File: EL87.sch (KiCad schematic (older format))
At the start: 289 parts, among them SW1 ESC, SW10 F12, SW11 ScrlLck, SW12 PauseBrk, SW13 1, SW14 F2, SW15 4, SW16 5, SW17 7, SW18 8, SW19 F8, SW2 F1, SW20 -, SW21 Backspace_2, SW22 PrntScrn, SW23 /, SW24 extra, SW25 `, SW26 2, SW27 W, SW28 6, SW29 Y, SW3 F3, SW30 9, SW31 F9, SW32 =, SW33 ], SW34 NumLock, SW35 8, SW36 *, SW37 Tab_15, SW38 3, SW39 E, SW4 F4, SW40 R, SW41 U, SW42 I, SW43 0, SW44 P, SW45 \\_15, SW46 7, SW47 5, SW48 -, SW49 Caps_175, SW5 F5, SW50 Q, SW51 S, SW52 T, SW53 H, SW54 J, SW55 O, SW56 [, SW57 ', SW58 4, SW59 2, SW6 F6, SW60 9, SW61 Shift_225, SW62 A, SW63 D, SW64 F, SW65 B, SW66 K, SW67 L, SW68 ;, SW69 Enter_225, SW7 F7, SW70 1, SW71 3, SW72 +_2V, SW73 Ctl_125, SW74 Z, SW75 X, SW76 G, SW77 N, SW78 M, SW79 >, SW8 F10, SW80 /, SW81 Shift_275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

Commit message: updated bottom row to be standard arranged LEDs to snake from top left to bottom left updated values to match key size cleaned up silk screens
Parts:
- SW25: value ` -> GRAVE
- SW57: value ' -> APOSTROPHE
- SW85: value OS -> OS_125; footprint Keyboard:MXALPS -> Keyboard:MXALPS_1.25U
- SW89: value SPACE_7 -> SPACE_625; footprint Keyboard:MXALPS_7U -> Keyboard:MXALPS_6.25U
- SW92: value Fn -> Fn_125; footprint Keyboard:MXALPS -> Keyboard:MXALPS_1.25U
- SW93: value Menu -> Menu_125; footprint Keyboard:MXALPS -> Keyboard:MXALPS_1.25U
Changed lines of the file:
@@
 P 4450 3000
 F 0 "SW25" H 4450 2900 60  0000 C CNN
-F 1 "`" H 4450 3000 60  0001 C CNN
+F 1 "GRAVE" H 4450 3000 60  0001 C CNN
 F 2 "Keyboard:MXALPS" H 4450 3000 60  0001 C CNN
 F 3 "" H 4450 3000 60  0000 C CNN
@@
 P 12450 5000
 F 0 "SW57" H 12450 4900 60  0000 C CNN
-F 1 "'" H 12450 5000 60  0001 C CNN
+F 1 "APOSTROPHE" H 12450 5000 60  0001 C CNN
 F 2 "Keyboard:MXALPS" H 12450 5000 60  0001 C CNN
 F 3 "" H 12450 5000 60  0000 C CNN
@@
 P 8450 8000
 F 0 "SW89" H 8450 7900 60  0000 C CNN
-F 1 "SPACE_7" H 8450 8000 60  0001 C CNN
-F 2 "Keyboard:MXALPS_7U" H 8450 8000 60  0001 C CNN
+F 1 "SPACE_625" H 8450 8000 60  0001 C CNN
+F 2 "Keyboard:MXALPS_6.25U" H 8450 8000 60  0001 C CNN
 F 3 "" H 8450 8000 60  0000 C CNN
 	1    8450 8000
@@
 P 12450 8000
 F 0 "SW93" H 12450 7900 60  0000 C CNN
-F 1 "Menu" H 12450 8000 60  0001 C CNN
-F 2 "Keyboard:MXALPS" H 12450 8000 60  0001 C CNN
+F 1 "Menu_125" H 12450 8000 60  0001 C CNN
+F 2 "Keyboard:MXALPS_1.25U" H 12450 8000 60  0001 C CNN
 F 3 "" H 12450 8000 60  0000 C CNN
 	1    12450 8000
@@
 P 4450 8000
 F 0 "SW85" H 4450 7900 60  0000 C CNN
-F 1 "OS" H 4450 8000 60  0001 C CNN
-F 2 "Keyboard:MXALPS" H 4450 8000 60  0001 C CNN
+F 1 "OS_125" H 4450 8000 60  0001 C CNN
+F 2 "Keyboard:MXALPS_1.25U" H 4450 8000 60  0001 C CNN
 F 3 "" H 4450 8000 60  0000 C CNN
 	1    4450 8000
@@
 P 11450 8000
 F 0 "SW92" H 11450 7900 60  0000 C CNN
-F 1 "Fn" H 11450 8000 60  0001 C CNN
-F 2 "Keyboard:MXALPS" H 11450 8000 60  0001 C CNN
+F 1 "Fn_125" H 11450 8000 60  0001 C CNN
+F 2 "Keyboard:MXALPS_1.25U" H 11450 8000 60  0001 C CNN
 F 3 "" H 11450 8000 60  0000 C CNN
 	1    11450 8000

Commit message: changed matrix to have columns follow physical rows to make layout easier to understand
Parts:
- added C1, C10, C11, C12, C13, C14, C15, C16, C17, C18, C19, C2, C20, C21, C22, C23, C24, C25, C26, C27, C28, C29, C3, C30, C31, C32, C33, C34, C35, C36, C37, C38, C39, C4, C40, C41, C42, C43, C44, C45, C46, C47, C48, C49, C5, C50, C51, C52, C53, C54, C55, C56, C57, C58, C59, C6, C60, C61, C62, C63, C64, C65, C66, C67, C68, C69, C7, C70, C71, C72, C73, C74, C75, C76, C77, C78, C79, C8, C80, C81, C82, C83, C84, C85, C86, C87, C88, C89, C9, C90, C91, C92, C93, C94, C95, C96: 100nF, Keebio-Parts:MX-1U-0805, symbol device:C_Small
- SW10: value F12 -> C
- SW11: value ScrlLck -> Shift_275; footprint Keyboard:MXALPS -> Keyboard:MXALPS_2.75U
- SW12: value PauseBrk -> Space_625; footprint Keyboard:MXALPS -> Keyboard:MXALPS_6.25U
- SW13: value 1 -> F1
- SW14: value F2 -> F9
- SW15: value 4 -> GRAVE
- SW16: value 5 -> 8
- SW17: value 7 -> PgUp
- SW18: value 8 -> Y
- SW19: value F8 -> 7
- SW2: value F1 -> F8
- SW20: value - -> F
- SW21: value Backspace_2 -> ENTER_225; footprint Keyboard:MXALPS_2U -> Keyboard:MXALPS_2.25U
- SW22: value PrntScrn -> V
- SW23: value / -> 1
- SW24: value extra -> Alt_125; footprint Keyboard:MXALPS -> Keyboard:MXALPS_1.25U
- SW25: value GRAVE -> F2
- SW26: value 2 -> F10
- SW27: value W -> 1
- SW28: value 6 -> 9
- SW29: value Y -> -
- SW3: value F3 -> ExtNL
- SW30: value 9 -> U
- SW31: value F9 -> 8
- SW32: value = -> G
- SW33: value ] -> 4
- SW34: value NumLock -> B
- SW35: value 8 -> 2
- SW36: value * -> FN_125; footprint Keyboard:MXALPS -> Keyboard:MXALPS_1.25U
- SW37: value Tab_15 -> F3; footprint Keyboard:MXALPS_1.5U -> Keyboard:MXALPS
- SW38: value 3 -> F11
- SW39: value E -> 2
- SW4: value F4 -> 7
- SW40: value R -> 0
- SW41: value U -> Tab_15; footprint Keyboard:MXALPS -> Keyboard:MXALPS_1.5U
- SW43: value 0 -> 9
- SW44: value P -> H
- SW45: value \\_15 -> 5; footprint Keyboard:MXALPS_1.5U -> Keyboard:MXALPS
- SW46: value 7 -> N
- SW47: value 5 -> 3
- SW48: value - -> Menu_125; footprint Keyboard:MXALPS -> Keyboard:MXALPS_1.25U
- SW49: value Caps_175 -> F4; footprint Keyboard:MXALPS_1.75U -> Keyboard:MXALPS
- SW5: value F5 -> Home
- SW50: value Q -> F12
- SW51: value S -> 3
- SW52: value T -> -
- SW53: value H -> Q
- SW54: value J -> O
- SW55: value O -> +
- SW56: value [ -> J
- SW57: value APOSTROPHE -> 6
- SW58: value 4 -> M
- SW59: value 2 -> ENTER_2V
- SW6: value F6 -> T
- SW60: value 9 -> Ctrl_125; footprint Keyboard:MXALPS -> Keyboard:MXALPS_1.25U
- SW61: value Shift_225 -> F5; footprint Keyboard:MXALPS_2.25U -> Keyboard:MXALPS
- SW62: value A -> PrtScr
- SW63: value D -> 4
- SW64: value F -> =
- SW65: value B -> W
- SW66: value K -> P
- SW67: value L -> Caps; footprint Keyboard:MXALPS -> Keyboard:MXALPS_1.75U
- SW68: value ; -> K
- SW69: value Enter_225 -> Shift_225
- SW7: value F7 -> \\_15; footprint Keyboard:MXALPS -> Keyboard:MXALPS_1.5U
- SW70: value 1 -> ,
- SW71: value 3 -> Crtl_125; footprint Keyboard:MXALPS -> Keyboard:MXALPS_1.25U
- SW72: value +_2V -> 0
- SW73: value Ctl_125 -> F6; footprint Keyboard:MXALPS_1.25U -> Keyboard:MXALPS
- SW74: value Z -> ScrlLck
- SW75: value X -> 5
- SW76: value G -> BckSpc_2; footprint Keyboard:MXALPS -> Keyboard:MXALPS_2U
- SW77: value N -> E
- SW78: value M -> [
- SW79: value > -> A
- SW8: value F10 -> D
- SW80: value / -> L
- SW81: value Shift_275 -> Z; footprint Keyboard:MXALPS_2.75U -> Keyboard:MXALPS
- SW82: value 0 -> .
- SW83: value 00 -> OS_125; footprint Keyboard:MXALPS -> Keyboard:MXALPS_1.25U
- SW84: value 6 -> 00
- SW85: value OS_125 -> F7; footprint Keyboard:MXALPS_1.25U -> Keyboard:MXALPS
- SW86: value Alt_125 -> PsBrk; footprint Keyboard:MXALPS_1.25U -> Keyboard:MXALPS
- SW87: value C -> 6
- SW88: value V -> Insert
- SW89: value SPACE_625 -> R; footprint Keyboard:MXALPS_6.25U -> Keyboard:MXALPS
- SW9: value F11 -> APOSTROPHE
- SW90: value < -> ]
- SW91: value Alt_125 -> S; footprint Keyboard:MXALPS_1.25U -> Keyboard:MXALPS
- SW92: value Fn_125 -> ;; footprint Keyboard:MXALPS_1.25U -> Keyboard:MXALPS
- SW93: value Menu_125 -> X; footprint Keyboard:MXALPS_1.25U -> Keyboard:MXALPS
- SW94: value Ctrl_125 -> /; footprint Keyboard:MXALPS_1.25U -> Keyboard:MXALPS
- SW95: value . -> Alt_125; footprint Keyboard:MXALPS -> Keyboard:MXALPS_1.25U
- SW96: value Enter_2V -> .

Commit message: Added alternative layouts
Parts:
- removed C14, C15, C16, C17, C33, C34, C35, C51, C52, C53, C69, C83, C84, C85, C95, C96: 100nF, Keebio-Parts:MX-1U-0805, symbol device:C_Small
- removed D11, D12, D23, D24, D27, D35, D36, D47, D48, D59, D60, D71, D72, D83, D84, D95, D96: D, SMD Diodes:D_SOD-123_HandSoldering, symbol device:D
- removed LED14, LED15, LED16, LED17, LED33, LED34, LED35, LED51, LED52, LED53, LED69, LED83, LED84, LED85, LED95, LED96: SK6812Mini-E, Keebio-Parts:MX-1U-KS6812Mini-E, symbol device:SK6812Mini-E
- removed SW11: Shift_275, Keyboard:MXALPS_2.75U, symbol cherrymx:MX_LED
- removed SW12: Space_625, Keyboard:MXALPS_6.25U, symbol cherrymx:MX_LED
- removed SW23: 1, Keyboard:MXALPS, symbol cherrymx:MX_LED
- removed SW24, SW95: Alt_125, Keyboard:MXALPS_1.25U, symbol cherrymx:MX_LED
- removed SW35: 2, Keyboard:MXALPS, symbol cherrymx:MX_LED
- removed SW36: FN_125, Keyboard:MXALPS_1.25U, symbol cherrymx:MX_LED
- removed SW47: 3, Keyboard:MXALPS, symbol cherrymx:MX_LED
- removed SW48: Menu_125, Keyboard:MXALPS_1.25U, symbol cherrymx:MX_LED
- removed SW59: ENTER_2V, Keyboard:MXALPS, symbol cherrymx:MX_LED
- removed SW60: Ctrl_125, Keyboard:MXALPS_1.25U, symbol cherrymx:MX_LED
- removed SW71: Crtl_125, Keyboard:MXALPS_1.25U, symbol cherrymx:MX_LED
- removed SW72: 0, Keyboard:MXALPS, symbol cherrymx:MX_LED
- removed SW83: OS_125, Keyboard:MXALPS_1.25U, symbol cherrymx:MX_LED
- removed SW84: 00, Keyboard:MXALPS, symbol cherrymx:MX_LED
- removed SW96: ., Keyboard:MXALPS, symbol cherrymx:MX_LED
- added C100, C81, C82, C83, C84, C85, C86, C87, C88, C89, C90, C91, C92, C93, C94, C95, C96, C97, C98, C99, C_97: 100nF, Keebio-Parts:MX-1U-0805, symbol EL87-rescue:C_Small-device
- added D100, D81, D82, D84, D85, D86, D87, D88, D89, D90, D91, D92, D93, D94, D95, D96, D97, D98, D99: D, SMD Diodes:D_SOD-123_HandSoldering, symbol EL87-rescue:D-device
- added LED100, LED81, LED82, LED83, LED84, LED85, LED86, LED87, LED88, LED89, LED90, LED91, LED92, LED93, LED94, LED95, LED96, LED97, LED98, LED99, LED_97: SK6812Mini-E, Keebio-Parts:MX-1U-KS6812Mini-E, symbol EL87-rescue:SK6812Mini-E-device
- added SW100: CTRL_1.25, Keyboard:MXALPS_1.25U, symbol EL87-rescue:MX_LED-cherrymx
- added SW81, SW90: ., Keyboard:MXALPS, symbol EL87-rescue:MX_LED-cherrymx
- added SW82: /, Keyboard:MXALPS, symbol EL87-rescue:MX_LED-cherrymx
- added SW83: Shift_split_1.75, Keyboard:MXALPS_1.75U, symbol EL87-rescue:MX_LED-cherrymx
- added SW84: Shift_2.75, Keyboard:MXALPS_2.75U, symbol EL87-rescue:MX_LED-cherrymx
- added SW85: Shift_split_fn, Keyboard:MXALPS, symbol EL87-rescue:MX_LED-cherrymx
- added SW86: 1, Keyboard:MXALPS, symbol EL87-rescue:MX_LED-cherrymx
- added SW87: 2, Keyboard:MXALPS, symbol EL87-rescue:MX_LED-cherrymx
- added SW88: 3, Keyboard:MXALPS, symbol EL87-rescue:MX_LED-cherrymx
- added SW89: Enter, Keyboard:MXALPS, symbol EL87-rescue:MX_LED-cherrymx
- added SW91: 00, Keyboard:MXALPS, symbol EL87-rescue:MX_LED-cherrymx
- added SW92: 0, Keyboard:MXALPS, symbol EL87-rescue:MX_LED-cherrymx
- added SW93: Ctrl_1.25, Keyboard:MXALPS_1.25U, symbol EL87-rescue:MX_LED-cherrymx
- added SW94: MENU_1.25, Keyboard:MXALPS_1.25U, symbol EL87-rescue:MX_LED-cherrymx
- added SW95, SW99: GUI_1.25, Keyboard:MXALPS_1.25U, symbol EL87-rescue:MX_LED-cherrymx
- added SW96, SW98: ALT_1.25, Keyboard:MXALPS_1.25U, symbol EL87-rescue:MX_LED-cherrymx
- added SW97: SPACE_6.25, Keyboard:MXALPS_6.25U, symbol EL87-rescue:MX_LED-cherrymx
- added SW_100, SW_93: CTRL_1.5, Keyboard:MXALPS_1.5U, symbol EL87-rescue:MX_LED-cherrymx
- added SW_94, SW_99: GUI, Keyboard:MXALPS, symbol EL87-rescue:MX_LED-cherrymx
- added SW_95, SW_98: ALT_1.5, Keyboard:MXALPS_1.5U, symbol EL87-rescue:MX_LED-cherrymx
- added SW_97: SPACE_7, Keyboard:MXALPS_7U, symbol EL87-rescue:MX_LED-cherrymx
- C1, C2, C26, C27, C3, C4, C49, C5, C6, C7: symbol device:C_Small -> EL87-rescue:C_Small-device
- C10: renamed from C11; symbol device:C_Small -> EL87-rescue:C_Small-device
- C11: renamed from C18; symbol device:C_Small -> EL87-rescue:C_Small-device
- C12: renamed from C19; symbol device:C_Small -> EL87-rescue:C_Small-device
- C13: renamed from C20; symbol device:C_Small -> EL87-rescue:C_Small-device
- C14: renamed from C21; symbol device:C_Small -> EL87-rescue:C_Small-device
- C15: renamed from C22; symbol device:C_Small -> EL87-rescue:C_Small-device
- C16: renamed from C25; symbol device:C_Small -> EL87-rescue:C_Small-device
- C17: renamed from C8; symbol device:C_Small -> EL87-rescue:C_Small-device
- C18: renamed from C28; symbol device:C_Small -> EL87-rescue:C_Small-device
- C19: renamed from C29; symbol device:C_Small -> EL87-rescue:C_Small-device
- C20: renamed from C12; symbol device:C_Small -> EL87-rescue:C_Small-device
- C21: renamed from C36; symbol device:C_Small -> EL87-rescue:C_Small-device
- C22: renamed from C37; symbol device:C_Small -> EL87-rescue:C_Small-device
- C23: renamed from C38; symbol device:C_Small -> EL87-rescue:C_Small-device
- C24: renamed from C39; symbol device:C_Small -> EL87-rescue:C_Small-device
- C25: renamed from C23; symbol device:C_Small -> EL87-rescue:C_Small-device
- C28: renamed from C46; symbol device:C_Small -> EL87-rescue:C_Small-device
- C29: renamed from C30; symbol device:C_Small -> EL87-rescue:C_Small-device
- C30: renamed from C13; symbol device:C_Small -> EL87-rescue:C_Small-device
- C31: renamed from C54; symbol device:C_Small -> EL87-rescue:C_Small-device
- C32: renamed from C55; symbol device:C_Small -> EL87-rescue:C_Small-device
- C33: renamed from C56; symbol device:C_Small -> EL87-rescue:C_Small-device
- C34: renamed from C40; symbol device:C_Small -> EL87-rescue:C_Small-device
- C35: renamed from C24; symbol device:C_Small -> EL87-rescue:C_Small-device
- C36: renamed from C44; symbol device:C_Small -> EL87-rescue:C_Small-device
- C37: renamed from C45; symbol device:C_Small -> EL87-rescue:C_Small-device
- C38: renamed from C47; symbol device:C_Small -> EL87-rescue:C_Small-device
- C39: renamed from C48; symbol device:C_Small -> EL87-rescue:C_Small-device
- C40: renamed from C31; symbol device:C_Small -> EL87-rescue:C_Small-device
- C41: renamed from C70; symbol device:C_Small -> EL87-rescue:C_Small-device
- C42: renamed from C71; symbol device:C_Small -> EL87-rescue:C_Small-device
- C43: renamed from C57; symbol device:C_Small -> EL87-rescue:C_Small-device
- C44: renamed from C41; symbol device:C_Small -> EL87-rescue:C_Small-device
- C45: renamed from C42; symbol device:C_Small -> EL87-rescue:C_Small-device
- C46: renamed from C62; symbol device:C_Small -> EL87-rescue:C_Small-device
- C47: renamed from C63; symbol device:C_Small -> EL87-rescue:C_Small-device
- C48: renamed from C65; symbol device:C_Small -> EL87-rescue:C_Small-device
- C50: renamed from C32; symbol device:C_Small -> EL87-rescue:C_Small-device
- C51: renamed from C86; symbol device:C_Small -> EL87-rescue:C_Small-device
- C52: renamed from C72; symbol device:C_Small -> EL87-rescue:C_Small-device
- C53: renamed from C58; symbol device:C_Small -> EL87-rescue:C_Small-device
- C54: renamed from C59; symbol device:C_Small -> EL87-rescue:C_Small-device
- C55: renamed from C43; symbol device:C_Small -> EL87-rescue:C_Small-device
- C56: renamed from C78; symbol device:C_Small -> EL87-rescue:C_Small-device
- C57: renamed from C64; symbol device:C_Small -> EL87-rescue:C_Small-device
- C58: renamed from C92; symbol device:C_Small -> EL87-rescue:C_Small-device
- C59: renamed from C66; symbol device:C_Small -> EL87-rescue:C_Small-device
- C60: renamed from C50; symbol device:C_Small -> EL87-rescue:C_Small-device
- C61: renamed from C87; symbol device:C_Small -> EL87-rescue:C_Small-device
- C62: renamed from C73; symbol device:C_Small -> EL87-rescue:C_Small-device
- C63: renamed from C74; symbol device:C_Small -> EL87-rescue:C_Small-device
- C64: renamed from C60; symbol device:C_Small -> EL87-rescue:C_Small-device
- C65: renamed from C61; symbol device:C_Small -> EL87-rescue:C_Small-device
- C66: renamed from C79; symbol device:C_Small -> EL87-rescue:C_Small-device
- C67: renamed from C80; symbol device:C_Small -> EL87-rescue:C_Small-device
- C68: renamed from C93; symbol device:C_Small -> EL87-rescue:C_Small-device
- C69: renamed from C81; symbol device:C_Small -> EL87-rescue:C_Small-device
- C70: renamed from C67; symbol device:C_Small -> EL87-rescue:C_Small-device
- C71: renamed from C88; symbol device:C_Small -> EL87-rescue:C_Small-device
- C72: renamed from C89; symbol device:C_Small -> EL87-rescue:C_Small-device
- C73: renamed from C75; symbol device:C_Small -> EL87-rescue:C_Small-device
- C74: renamed from C76; symbol device:C_Small -> EL87-rescue:C_Small-device
- C75: renamed from C77; symbol device:C_Small -> EL87-rescue:C_Small-device
- C76: renamed from C90; symbol device:C_Small -> EL87-rescue:C_Small-device
- C77: renamed from C91; symbol device:C_Small -> EL87-rescue:C_Small-device
- C78: renamed from C94; symbol device:C_Small -> EL87-rescue:C_Small-device
- C79: renamed from C82; symbol device:C_Small -> EL87-rescue:C_Small-device
- C8: renamed from C9; symbol device:C_Small -> EL87-rescue:C_Small-device
- C80: renamed from C68; symbol device:C_Small -> EL87-rescue:C_Small-device
- C9: renamed from C10; symbol device:C_Small -> EL87-rescue:C_Small-device
- D1, D10, D2, D3, D4, D5, D6, D7, D8, D9: symbol device:D -> EL87-rescue:D-device
- D11: renamed from D13; symbol device:D -> EL87-rescue:D-device
- D12: renamed from D14; symbol device:D -> EL87-rescue:D-device
- D13: renamed from D15; symbol device:D -> EL87-rescue:D-device
- D14: renamed from D16; symbol device:D -> EL87-rescue:D-device
- D15: renamed from D17; symbol device:D -> EL87-rescue:D-device
- D16: renamed from D18; symbol device:D -> EL87-rescue:D-device
- D17: renamed from D19; symbol device:D -> EL87-rescue:D-device
- D18: renamed from D20; symbol device:D -> EL87-rescue:D-device
- D19: renamed from D21; symbol device:D -> EL87-rescue:D-device
- D20: renamed from D22; symbol device:D -> EL87-rescue:D-device
- D21: renamed from D25; symbol device:D -> EL87-rescue:D-device
- D22: renamed from D26; symbol device:D -> EL87-rescue:D-device
- D24: renamed from D28; symbol device:D -> EL87-rescue:D-device
- D25: renamed from D29; symbol device:D -> EL87-rescue:D-device
- D26: renamed from D30; symbol device:D -> EL87-rescue:D-device
- D27: renamed from D31; symbol device:D -> EL87-rescue:D-device
- D28: renamed from D32; symbol device:D -> EL87-rescue:D-device
- D29: renamed from D33; symbol device:D -> EL87-rescue:D-device
- D30: renamed from D34; symbol device:D -> EL87-rescue:D-device
- D31: renamed from D37; symbol device:D -> EL87-rescue:D-device
- D32: renamed from D38; symbol device:D -> EL87-rescue:D-device
- D33: renamed from D39; symbol device:D -> EL87-rescue:D-device
- D34: renamed from D40; symbol device:D -> EL87-rescue:D-device
- D35: renamed from D41; symbol device:D -> EL87-rescue:D-device
- D36: renamed from D42; symbol device:D -> EL87-rescue:D-device
- D37: renamed from D43; symbol device:D -> EL87-rescue:D-device
- D38: renamed from D44; symbol device:D -> EL87-rescue:D-device
- D39: renamed from D45; symbol device:D -> EL87-rescue:D-device
- D40: renamed from D46; symbol device:D -> EL87-rescue:D-device
- D41: renamed from D49; symbol device:D -> EL87-rescue:D-device
- D42: renamed from D50; symbol device:D -> EL87-rescue:D-device
- D43: renamed from D51; symbol device:D -> EL87-rescue:D-device
- D44: renamed from D52; symbol device:D -> EL87-rescue:D-device
- D45: renamed from D53; symbol device:D -> EL87-rescue:D-device
- D46: renamed from D54; symbol device:D -> EL87-rescue:D-device
- D47: renamed from D55; symbol device:D -> EL87-rescue:D-device
- D48: renamed from D56; symbol device:D -> EL87-rescue:D-device
- D49: renamed from D57; symbol device:D -> EL87-rescue:D-device
- D50: renamed from D58; symbol device:D -> EL87-rescue:D-device
- D51: renamed from D61; symbol device:D -> EL87-rescue:D-device
- D52: renamed from D62; symbol device:D -> EL87-rescue:D-device
- D53: renamed from D63; symbol device:D -> EL87-rescue:D-device
- D54: renamed from D64; symbol device:D -> EL87-rescue:D-device
- D55: renamed from D65; symbol device:D -> EL87-rescue:D-device
- D56: renamed from D66; symbol device:D -> EL87-rescue:D-device
- D57: renamed from D67; symbol device:D -> EL87-rescue:D-device
- D58: renamed from D68; symbol device:D -> EL87-rescue:D-device
- D59: renamed from D69; symbol device:D -> EL87-rescue:D-device
- D60: renamed from D70; symbol device:D -> EL87-rescue:D-device
- D61: renamed from D73; symbol device:D -> EL87-rescue:D-device
- D62: renamed from D74; symbol device:D -> EL87-rescue:D-device
- D63: renamed from D75; symbol device:D -> EL87-rescue:D-device
- D64: renamed from D76; symbol device:D -> EL87-rescue:D-device
- D65: renamed from D77; symbol device:D -> EL87-rescue:D-device
- D66: renamed from D78; symbol device:D -> EL87-rescue:D-device
- D67: renamed from D79; symbol device:D -> EL87-rescue:D-device
- D68: renamed from D80; symbol device:D -> EL87-rescue:D-device
- D69: renamed from D81; symbol device:D -> EL87-rescue:D-device
- D70: renamed from D82; symbol device:D -> EL87-rescue:D-device
- D71: renamed from D85; symbol device:D -> EL87-rescue:D-device
- D72: renamed from D86; symbol device:D -> EL87-rescue:D-device
- D73: renamed from D87; symbol device:D -> EL87-rescue:D-device
- D74: renamed from D88; symbol device:D -> EL87-rescue:D-device
- D75: renamed from D89; symbol device:D -> EL87-rescue:D-device
- D76: renamed from D90; symbol device:D -> EL87-rescue:D-device
- D77: renamed from D91; symbol device:D -> EL87-rescue:D-device
- D78: renamed from D92; symbol device:D -> EL87-rescue:D-device
- D79: renamed from D93; symbol device:D -> EL87-rescue:D-device
- D80: renamed from D94; symbol device:D -> EL87-rescue:D-device
- LED1, LED2, LED26, LED27, LED3, LED4, LED49, LED5, LED6, LED7: symbol device:SK6812Mini-E -> EL87-rescue:SK6812Mini-E-device
- LED10: renamed from LED11; symbol device:SK6812Mini-E -> EL87-rescue:SK6812Mini-E-device
- LED11: renamed from LED18; symbol device:SK6812Mini-E -> EL87-rescue:SK6812Mini-E-device
- LED12: renamed from LED19; symbol device:SK6812Mini-E -> EL87-rescue:SK6812Mini-E-device
- LED13: renamed from LED20; symbol device:SK6812Mini-E -> EL87-rescue:SK6812Mini-E-device
- LED14: renamed from LED21; symbol device:SK6812Mini-E -> EL87-rescue:SK6812Mini-E-device
- LED15: renamed from LED22; symbol device:SK6812Mini-E -> EL87-rescue:SK6812Mini-E-device
- LED16: renamed from LED25; symbol device:SK6812Mini-E -> EL87-rescue:SK6812Mini-E-device
- LED17: renamed from LED8; symbol device:SK6812Mini-E -> EL87-rescue:SK6812Mini-E-device
- LED18: renamed from LED28; symbol device:SK6812Mini-E -> EL87-rescue:SK6812Mini-E-device
- LED19: renamed from LED29; symbol device:SK6812Mini-E -> EL87-rescue:SK6812Mini-E-device
- LED20: renamed from LED12; symbol device:SK6812Mini-E -> EL87-rescue:SK6812Mini-E-device
- LED21: renamed from LED36; symbol device:SK6812Mini-E -> EL87-rescue:SK6812Mini-E-device
- LED22: renamed from LED37; symbol device:SK6812Mini-E -> EL87-rescue:SK6812Mini-E-device
- LED23: renamed from LED38; symbol device:SK6812Mini-E -> EL87-rescue:SK6812Mini-E-device
- LED24: renamed from LED39; symbol device:SK6812Mini-E -> EL87-rescue:SK6812Mini-E-device
- LED25: renamed from LED23; symbol device:SK6812Mini-E -> EL87-rescue:SK6812Mini-E-device
- LED28: renamed from LED46; symbol device:SK6812Mini-E -> EL87-rescue:SK6812Mini-E-device
- LED29: renamed from LED30; symbol device:SK6812Mini-E -> EL87-rescue:SK6812Mini-E-device
- LED30: renamed from LED13; symbol device:SK6812Mini-E -> EL87-rescue:SK6812Mini-E-device
- LED31: renamed from LED54; symbol device:SK6812Mini-E -> EL87-rescue:SK6812Mini-E-device
- LED32: renamed from LED55; symbol device:SK6812Mini-E -> EL87-rescue:SK6812Mini-E-device
- LED33: renamed from LED56; symbol device:SK6812Mini-E -> EL87-rescue:SK6812Mini-E-device
- LED34: renamed from LED40; symbol device:SK6812Mini-E -> EL87-rescue:SK6812Mini-E-device
- LED35: renamed from LED24; symbol device:SK6812Mini-E -> EL87-rescue:SK6812Mini-E-device
- LED36: renamed from LED44; symbol device:SK6812Mini-E -> EL87-rescue:SK6812Mini-E-device
- LED37: renamed from LED45; symbol device:SK6812Mini-E -> EL87-rescue:SK6812Mini-E-device
- LED38: renamed from LED47; symbol device:SK6812Mini-E -> EL87-rescue:SK6812Mini-E-device
- LED39: renamed from LED48; symbol device:SK6812Mini-E -> EL87-rescue:SK6812Mini-E-device
- LED40: renamed from LED31; symbol device:SK6812Mini-E -> EL87-rescue:SK6812Mini-E-device
- LED41: renamed from LED70; symbol device:SK6812Mini-E -> EL87-rescue:SK6812Mini-E-device
- LED42: renamed from LED71; symbol device:SK6812Mini-E -> EL87-rescue:SK6812Mini-E-device
- LED43: renamed from LED57; symbol device:SK6812Mini-E -> EL87-rescue:SK6812Mini-E-device
- LED44: renamed from LED41; symbol device:SK6812Mini-E -> EL87-rescue:SK6812Mini-E-device
- LED45: renamed from LED42; symbol device:SK6812Mini-E -> EL87-rescue:SK6812Mini-E-device
- LED46: renamed from LED62; symbol device:SK6812Mini-E -> EL87-rescue:SK6812Mini-E-device
- LED47: renamed from LED63; symbol device:SK6812Mini-E -> EL87-rescue:SK6812Mini-E-device
- LED48: renamed from LED65; symbol device:SK6812Mini-E -> EL87-rescue:SK6812Mini-E-device
- LED50: renamed from LED32; symbol device:SK6812Mini-E -> EL87-rescue:SK6812Mini-E-device
- LED51: renamed from LED86; symbol device:SK6812Mini-E -> EL87-rescue:SK6812Mini-E-device
- LED52: renamed from LED72; symbol device:SK6812Mini-E -> EL87-rescue:SK6812Mini-E-device
- LED53: renamed from LED58; symbol device:SK6812Mini-E -> EL87-rescue:SK6812Mini-E-device
- LED54: renamed from LED59; symbol device:SK6812Mini-E -> EL87-rescue:SK6812Mini-E-device
- LED55: renamed from LED43; symbol device:SK6812Mini-E -> EL87-rescue:SK6812Mini-E-device
- LED56: renamed from LED78; symbol device:SK6812Mini-E -> EL87-rescue:SK6812Mini-E-device
- LED57: renamed from LED64; symbol device:SK6812Mini-E -> EL87-rescue:SK6812Mini-E-device
- LED58: renamed from LED92; symbol device:SK6812Mini-E -> EL87-rescue:SK6812Mini-E-device
- LED59: renamed from LED66; symbol device:SK6812Mini-E -> EL87-rescue:SK6812Mini-E-device
- LED60: renamed from LED50; symbol device:SK6812Mini-E -> EL87-rescue:SK6812Mini-E-device
- LED61: renamed from LED87; symbol device:SK6812Mini-E -> EL87-rescue:SK6812Mini-E-device
- LED62: renamed from LED73; symbol device:SK6812Mini-E -> EL87-rescue:SK6812Mini-E-device
- LED63: renamed from LED74; symbol device:SK6812Mini-E -> EL87-rescue:SK6812Mini-E-device
- LED64: renamed from LED60; symbol device:SK6812Mini-E -> EL87-rescue:SK6812Mini-E-device
- LED65: renamed from LED61; symbol device:SK6812Mini-E -> EL87-rescue:SK6812Mini-E-device
- LED66: renamed from LED79; symbol device:SK6812Mini-E -> EL87-rescue:SK6812Mini-E-device
- LED67: renamed from LED80; symbol device:SK6812Mini-E -> EL87-rescue:SK6812Mini-E-device
- LED68: renamed from LED93; symbol device:SK6812Mini-E -> EL87-rescue:SK6812Mini-E-device
- LED69: renamed from LED81; symbol device:SK6812Mini-E -> EL87-rescue:SK6812Mini-E-device
- LED70: renamed from LED67; symbol device:SK6812Mini-E -> EL87-rescue:SK6812Mini-E-device
- LED71: renamed from LED88; symbol device:SK6812Mini-E -> EL87-rescue:SK6812Mini-E-device
- LED72: renamed from LED89; symbol device:SK6812Mini-E -> EL87-rescue:SK6812Mini-E-device
- LED73: renamed from LED75; symbol device:SK6812Mini-E -> EL87-rescue:SK6812Mini-E-device
- LED74: renamed from LED76; symbol device:SK6812Mini-E -> EL87-rescue:SK6812Mini-E-device
- LED75: renamed from LED77; symbol device:SK6812Mini-E -> EL87-rescue:SK6812Mini-E-device
- LED76: renamed from LED90; symbol device:SK6812Mini-E -> EL87-rescue:SK6812Mini-E-device
- LED77: renamed from LED91; symbol device:SK6812Mini-E -> EL87-rescue:SK6812Mini-E-device
- LED78: renamed from LED94; symbol device:SK6812Mini-E -> EL87-rescue:SK6812Mini-E-device
- LED79: renamed from LED82; symbol device:SK6812Mini-E -> EL87-rescue:SK6812Mini-E-device
- LED8: renamed from LED9; symbol device:SK6812Mini-E -> EL87-rescue:SK6812Mini-E-device
- LED80: renamed from LED68; symbol device:SK6812Mini-E -> EL87-rescue:SK6812Mini-E-device
- LED9: renamed from LED10; symbol device:SK6812Mini-E -> EL87-rescue:SK6812Mini-E-device
- SW1: symbol cherrymx:MX_LED -> EL87-rescue:MX_LED-cherrymx
- SW10: value C -> F9; symbol cherrymx:MX_LED -> EL87-rescue:MX_LED-cherrymx
- SW11: renamed from SW13; value F1 -> F10; symbol cherrymx:MX_LED -> EL87-rescue:MX_LED-cherrymx
- SW12: renamed from SW14; value F9 -> F11; symbol cherrymx:MX_LED -> EL87-rescue:MX_LED-cherrymx
- SW13: renamed from SW15; value GRAVE -> F12; symbol cherrymx:MX_LED -> EL87-rescue:MX_LED-cherrymx
- SW14: renamed from SW16; value 8 -> PrtScrn; symbol cherrymx:MX_LED -> EL87-rescue:MX_LED-cherrymx
- SW15: renamed from SW17; value PgUp -> ScrlLck; symbol cherrymx:MX_LED -> EL87-rescue:MX_LED-cherrymx
- SW16: renamed from SW18; value Y -> PB; symbol cherrymx:MX_LED -> EL87-rescue:MX_LED-cherrymx
- SW17: renamed from SW19; value 7 -> NumLck; symbol cherrymx:MX_LED -> EL87-rescue:MX_LED-cherrymx
- SW18: renamed from SW20; value F -> -; symbol cherrymx:MX_LED -> EL87-rescue:MX_LED-cherrymx
- SW19: renamed from SW21; value ENTER_225 -> PgUp; footprint Keyboard:MXALPS_2.25U -> Keyboard:MXALPS; symbol cherrymx:MX_LED -> EL87-rescue:MX_LED-cherrymx
- SW2: value F8 -> F1; symbol cherrymx:MX_LED -> EL87-rescue:MX_LED-cherrymx
- SW20: renamed from SW22; value V -> Home; symbol cherrymx:MX_LED -> EL87-rescue:MX_LED-cherrymx
- SW21: renamed from SW25; value F2 -> Insert; symbol cherrymx:MX_LED -> EL87-rescue:MX_LED-cherrymx
- SW22: renamed from SW26; value F10 -> BckSpc_split; symbol cherrymx:MX_LED -> EL87-rescue:MX_LED-cherrymx
- SW24: renamed from SW28; value 9 -> BckSpc_Split_2; symbol cherrymx:MX_LED -> EL87-rescue:MX_LED-cherrymx
- SW25: renamed from SW29; value - -> =; symbol cherrymx:MX_LED -> EL87-rescue:MX_LED-cherrymx
- SW26: renamed from SW30; value U -> -; symbol cherrymx:MX_LED -> EL87-rescue:MX_LED-cherrymx
- SW27: renamed from SW31; value 8 -> 0; symbol cherrymx:MX_LED -> EL87-rescue:MX_LED-cherrymx
- SW28: renamed from SW32; value G -> 9; symbol cherrymx:MX_LED -> EL87-rescue:MX_LED-cherrymx
- SW29: renamed from SW33; value 4 -> 8; symbol cherrymx:MX_LED -> EL87-rescue:MX_LED-cherrymx
- SW3: value ExtNL -> F2; symbol cherrymx:MX_LED -> EL87-rescue:MX_LED-cherrymx
- SW30: renamed from SW34; value B -> 7; symbol cherrymx:MX_LED -> EL87-rescue:MX_LED-cherrymx
- SW31: renamed from SW37; value F3 -> 6; symbol cherrymx:MX_LED -> EL87-rescue:MX_LED-cherrymx
- SW32: renamed from SW38; value F11 -> 5; symbol cherrymx:MX_LED -> EL87-rescue:MX_LED-cherrymx
- SW33: renamed from SW39; value 2 -> 4; symbol cherrymx:MX_LED -> EL87-rescue:MX_LED-cherrymx
- SW34: renamed from SW40; value 0 -> 3; symbol cherrymx:MX_LED -> EL87-rescue:MX_LED-cherrymx
- SW35: renamed from SW41; value Tab_15 -> 2; footprint Keyboard:MXALPS_1.5U -> Keyboard:MXALPS; symbol cherrymx:MX_LED -> EL87-rescue:MX_LED-cherrymx
- SW36: renamed from SW42; value I -> 1; symbol cherrymx:MX_LED -> EL87-rescue:MX_LED-cherrymx
- SW37: renamed from SW43; value 9 -> GRAVE; symbol cherrymx:MX_LED -> EL87-rescue:MX_LED-cherrymx
- SW38: renamed from SW44; value H -> Tab_1.5; footprint Keyboard:MXALPS -> Keyboard:MXALPS_1.5U; symbol cherrymx:MX_LED -> EL87-rescue:MX_LED-cherrymx
- SW39: renamed from SW45; value 5 -> Q; symbol cherrymx:MX_LED -> EL87-rescue:MX_LED-cherrymx
- SW4: value 7 -> F3; symbol cherrymx:MX_LED -> EL87-rescue:MX_LED-cherrymx
- SW40: renamed from SW46; value N -> W; symbol cherrymx:MX_LED -> EL87-rescue:MX_LED-cherrymx
- SW41: renamed from SW49; value F4 -> E; symbol cherrymx:MX_LED -> EL87-rescue:MX_LED-cherrymx
- SW42: renamed from SW50; value F12 -> R; symbol cherrymx:MX_LED -> EL87-rescue:MX_LED-cherrymx
- SW43: renamed from SW51; value 3 -> T; symbol cherrymx:MX_LED -> EL87-rescue:MX_LED-cherrymx
- SW44: renamed from SW52; value - -> Y; symbol cherrymx:MX_LED -> EL87-rescue:MX_LED-cherrymx
- SW45: renamed from SW53; value Q -> U; symbol cherrymx:MX_LED -> EL87-rescue:MX_LED-cherrymx
- SW46: renamed from SW54; value O -> I; symbol cherrymx:MX_LED -> EL87-rescue:MX_LED-cherrymx
- SW47: renamed from SW55; value + -> O; symbol cherrymx:MX_LED -> EL87-rescue:MX_LED-cherrymx
- SW48: renamed from SW56; value J -> P; symbol cherrymx:MX_LED -> EL87-rescue:MX_LED-cherrymx
- SW49: renamed from SW57; value 6 -> [; symbol cherrymx:MX_LED -> EL87-rescue:MX_LED-cherrymx
- SW5: value Home -> F4; symbol cherrymx:MX_LED -> EL87-rescue:MX_LED-cherrymx
- SW50: renamed from SW58; value M -> ]; symbol cherrymx:MX_LED -> EL87-rescue:MX_LED-cherrymx
- SW51: renamed from SW61; value F5 -> \\; symbol cherrymx:MX_LED -> EL87-rescue:MX_LED-cherrymx
- SW52: renamed from SW62; value PrtScr -> DEL; symbol cherrymx:MX_LED -> EL87-rescue:MX_LED-cherrymx
- SW53: renamed from SW63; value 4 -> END; symbol cherrymx:MX_LED -> EL87-rescue:MX_LED-cherrymx
- SW54: renamed from SW64; value = -> PGDN; symbol cherrymx:MX_LED -> EL87-rescue:MX_LED-cherrymx
- SW55: renamed from SW65; value W -> +; symbol cherrymx:MX_LED -> EL87-rescue:MX_LED-cherrymx
- SW56: renamed from SW66; value P -> 6; symbol cherrymx:MX_LED -> EL87-rescue:MX_LED-cherrymx
- SW57: renamed from SW67; value Caps -> 5; symbol cherrymx:MX_LED -> EL87-rescue:MX_LED-cherrymx
- SW58: renamed from SW68; value K -> 4; symbol cherrymx:MX_LED -> EL87-rescue:MX_LED-cherrymx
- SW59: renamed from SW69; value Shift_225 -> Enter_2.25; symbol cherrymx:MX_LED -> EL87-rescue:MX_LED-cherrymx
- SW6: value T -> F5; symbol cherrymx:MX_LED -> EL87-rescue:MX_LED-cherrymx
- SW60: renamed from SW70; value , -> APOSTROPHE; symbol cherrymx:MX_LED -> EL87-rescue:MX_LED-cherrymx
- SW61: renamed from SW73; value F6 -> ;; symbol cherrymx:MX_LED -> EL87-rescue:MX_LED-cherrymx
- SW62: renamed from SW74; value ScrlLck -> L; symbol cherrymx:MX_LED -> EL87-rescue:MX_LED-cherrymx
- SW63: renamed from SW75; value 5 -> K; symbol cherrymx:MX_LED -> EL87-rescue:MX_LED-cherrymx
- SW64: renamed from SW76; value BckSpc_2 -> J; footprint Keyboard:MXALPS_2U -> Keyboard:MXALPS; symbol cherrymx:MX_LED -> EL87-rescue:MX_LED-cherrymx
- SW65: renamed from SW77; value E -> H; symbol cherrymx:MX_LED -> EL87-rescue:MX_LED-cherrymx
- SW66: renamed from SW78; value [ -> G; symbol cherrymx:MX_LED -> EL87-rescue:MX_LED-cherrymx
- SW67: renamed from SW79; value A -> F; symbol cherrymx:MX_LED -> EL87-rescue:MX_LED-cherrymx
- SW68: renamed from SW80; value L -> D; symbol cherrymx:MX_LED -> EL87-rescue:MX_LED-cherrymx
- SW69: renamed from SW81; value Z -> S; symbol cherrymx:MX_LED -> EL87-rescue:MX_LED-cherrymx
- SW7: value \\_15 -> F6; symbol cherrymx:MX_LED -> EL87-rescue:MX_LED-cherrymx
- SW70: renamed from SW82; value . -> A; symbol cherrymx:MX_LED -> EL87-rescue:MX_LED-cherrymx
- SW71: renamed from SW85; value F7 -> CAPS_1.75; footprint Keyboard:MXALPS -> Keyboard:MXALPS_1.75U; symbol cherrymx:MX_LED -> EL87-rescue:MX_LED-cherrymx
- SW72: renamed from SW86; value PsBrk -> SHIFT_2.25; footprint Keyboard:MXALPS -> Keyboard:MXALPS_2.25U; symbol cherrymx:MX_LED -> EL87-rescue:MX_LED-cherrymx
- SW73: renamed from SW87; value 6 -> Z; symbol cherrymx:MX_LED -> EL87-rescue:MX_LED-cherrymx
- SW74: renamed from SW88; value Insert -> X; symbol cherrymx:MX_LED -> EL87-rescue:MX_LED-cherrymx
- SW75: renamed from SW89; value R -> C; symbol cherrymx:MX_LED -> EL87-rescue:MX_LED-cherrymx
- SW76: renamed from SW90; value ] -> V; symbol cherrymx:MX_LED -> EL87-rescue:MX_LED-cherrymx
- SW77: renamed from SW91; value S -> B; symbol cherrymx:MX_LED -> EL87-rescue:MX_LED-cherrymx
- SW78: renamed from SW92; value ; -> N; symbol cherrymx:MX_LED -> EL87-rescue:MX_LED-cherrymx
- SW79: renamed from SW93; value X -> M; symbol cherrymx:MX_LED -> EL87-rescue:MX_LED-cherrymx
- SW8: value D -> F7; symbol cherrymx:MX_LED -> EL87-rescue:MX_LED-cherrymx
- SW80: renamed from SW94; value / -> ,; symbol cherrymx:MX_LED -> EL87-rescue:MX_LED-cherrymx
- SW9: value APOSTROPHE -> F8; symbol cherrymx:MX_LED -> EL87-rescue:MX_LED-cherrymx
- SW_22: renamed from SW27; value 1 -> BckSpc_2; footprint Keyboard:MXALPS -> Keyboard:MXALPS_2U; symbol cherrymx:MX_LED -> EL87-rescue:MX_LED-cherrymx
- U1: symbol proton_c:proton_c -> EL87-rescue:proton_c-proton_c
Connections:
- net labels added: SIG_100, SIG_97, SIG_98, SIG_99, row8, row9
- net labels removed: col10, col11
- wire segments 192 -> 215
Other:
- moved on the sheet: D1, D10, D11, D12, D13, D14, D15, D16, D17, D18, D19, D2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

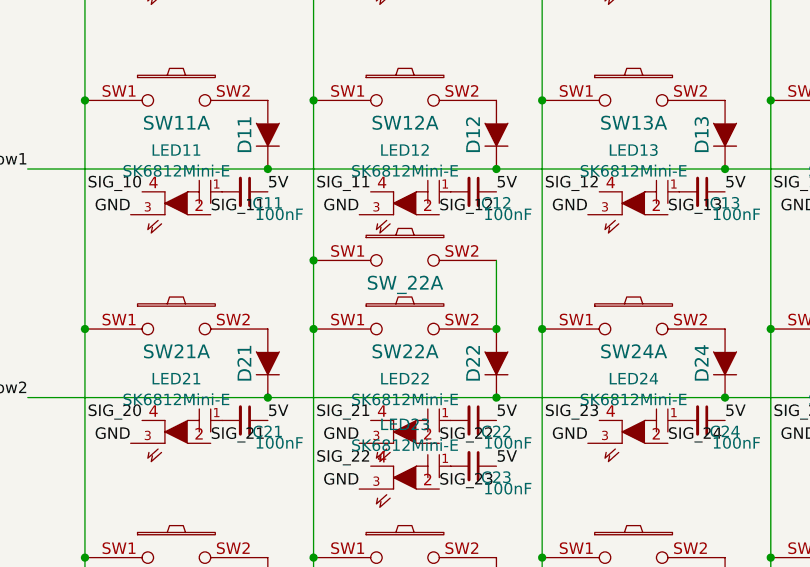
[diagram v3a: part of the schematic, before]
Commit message: verified LED layout
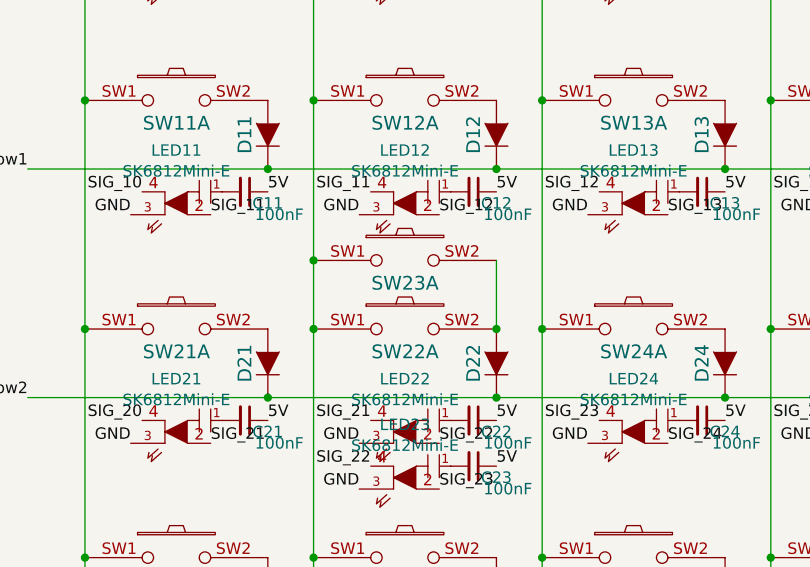
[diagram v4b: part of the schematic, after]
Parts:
- renumbered SW_22 to SW23
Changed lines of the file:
@@
 NoConn ~ 14300 3050
 $Comp
-L EL87-rescue:MX_LED-cherrymx SW_22
+L EL87-rescue:MX_LED-cherrymx SW23
 U 1 1 5F683568
 P 2600 2700
-F 0 "SW_22" H 2600 2600 60  0000 C CNN
+F 0 "SW23" H 2600 2600 60  0000 C CNN
 F 1 "BckSpc_2" H 2600 2700 60  0001 C CNN
 F 2 "Keyboard:MXALPS_2U" H 2600 2700 60  0001 C CNN
@@
 Wire Wire Line
 	1200 4000 1200 5000
-Wire Wire Line
-	6000 8300 7000 8300
 $Comp
 L EL87-rescue:MX_LED-cherrymx SW32
@@
 	1    0    0    -1
 $EndComp
+Wire Wire Line
+	6000 8300 7000 8300
 $EndSCHEMATC
